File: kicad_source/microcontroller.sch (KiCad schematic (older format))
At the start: 47 parts, among them CN1 Micro_SDCard, CN2 CONN_02X05, CN5 CONN_01X04, CN6 CONN_01X04, SW1 TAST_VER, SW2 TAST_VER, SW3 TAST_VER, SW4 TAST_VER, U1 W25Q80D, U2 ATECC608A, U3 FE310-G002, U8 BMA400, Y1 16MHz

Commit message: changed JTAG connector
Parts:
- CN2: footprint pin_headers:Pin_Header_Straight_2x05_Pitch1.27mm -> CON_samtec:FSH-105-04-L-DH-SL
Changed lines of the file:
@@
 F 0 "CN2" H 5600 6015 50  0000 C CNN
 F 1 "CONN_02X05" H 5600 5924 50  0000 C CNN
-F 2 "pin_headers:Pin_Header_Straight_2x05_Pitch1.27mm" H 5600 5600 50  0001 C CNN
+F 2 "CON_samtec:FSH-105-04-L-DH-SL" H 5600 5600 50  0001 C CNN
 F 3 "" H 5600 4400 50  0000 C CNN
 	1    5600 5600

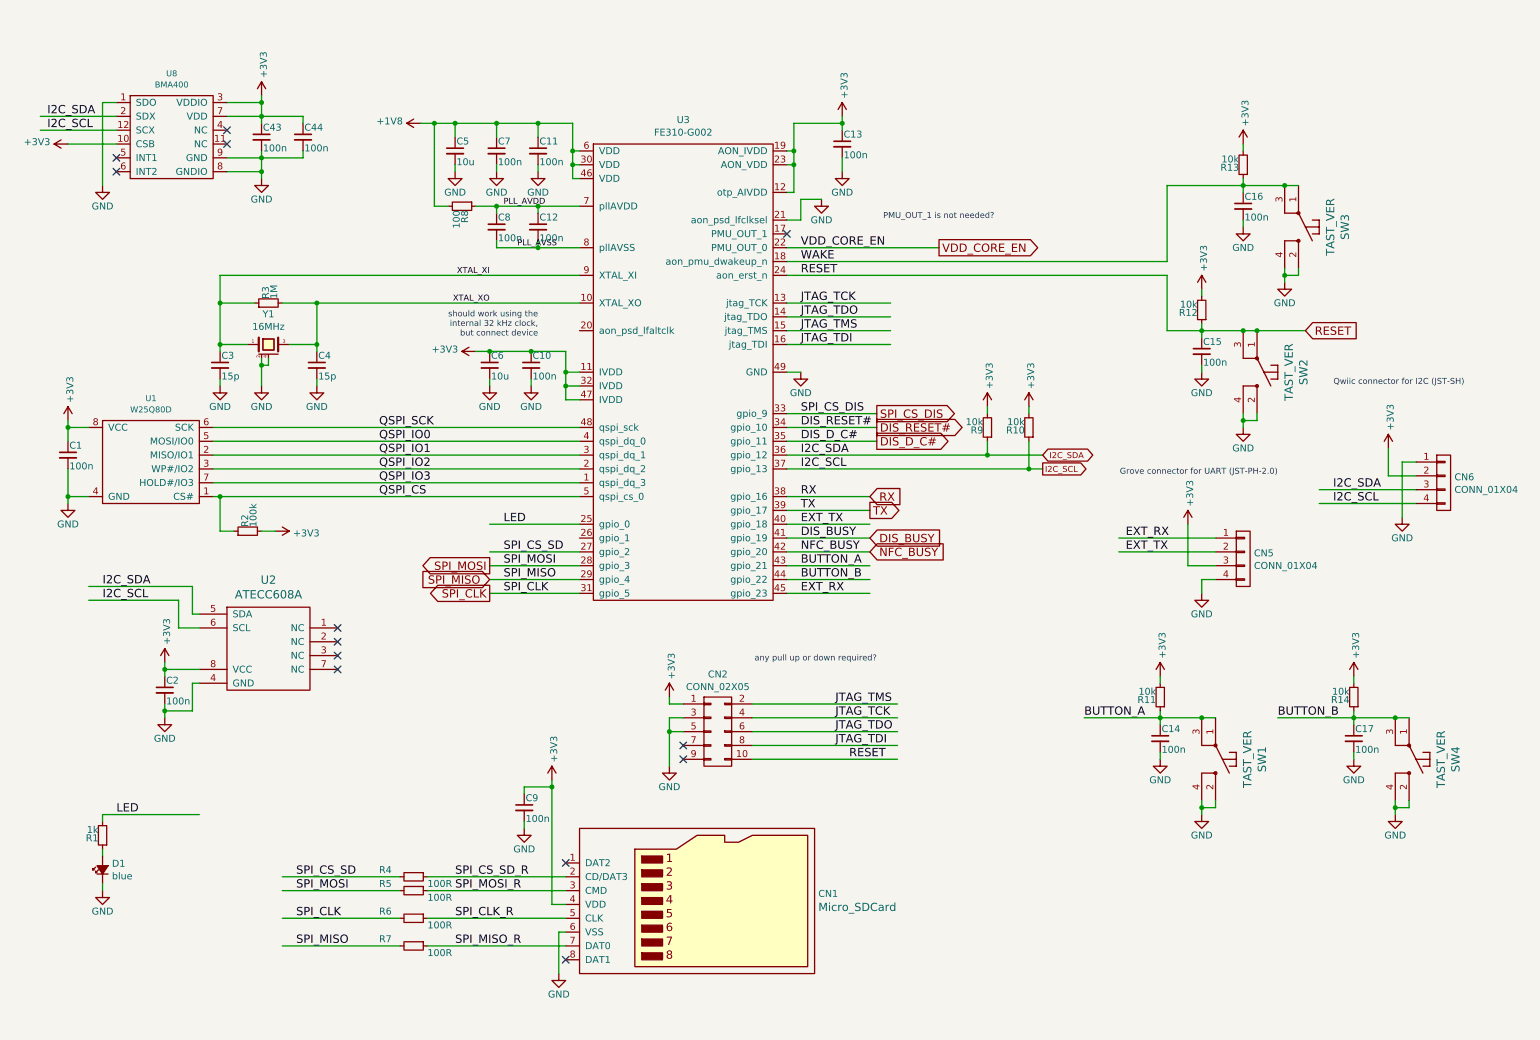
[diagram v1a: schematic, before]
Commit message: used small side switch for reset, added expansion connector,changed mounting holes
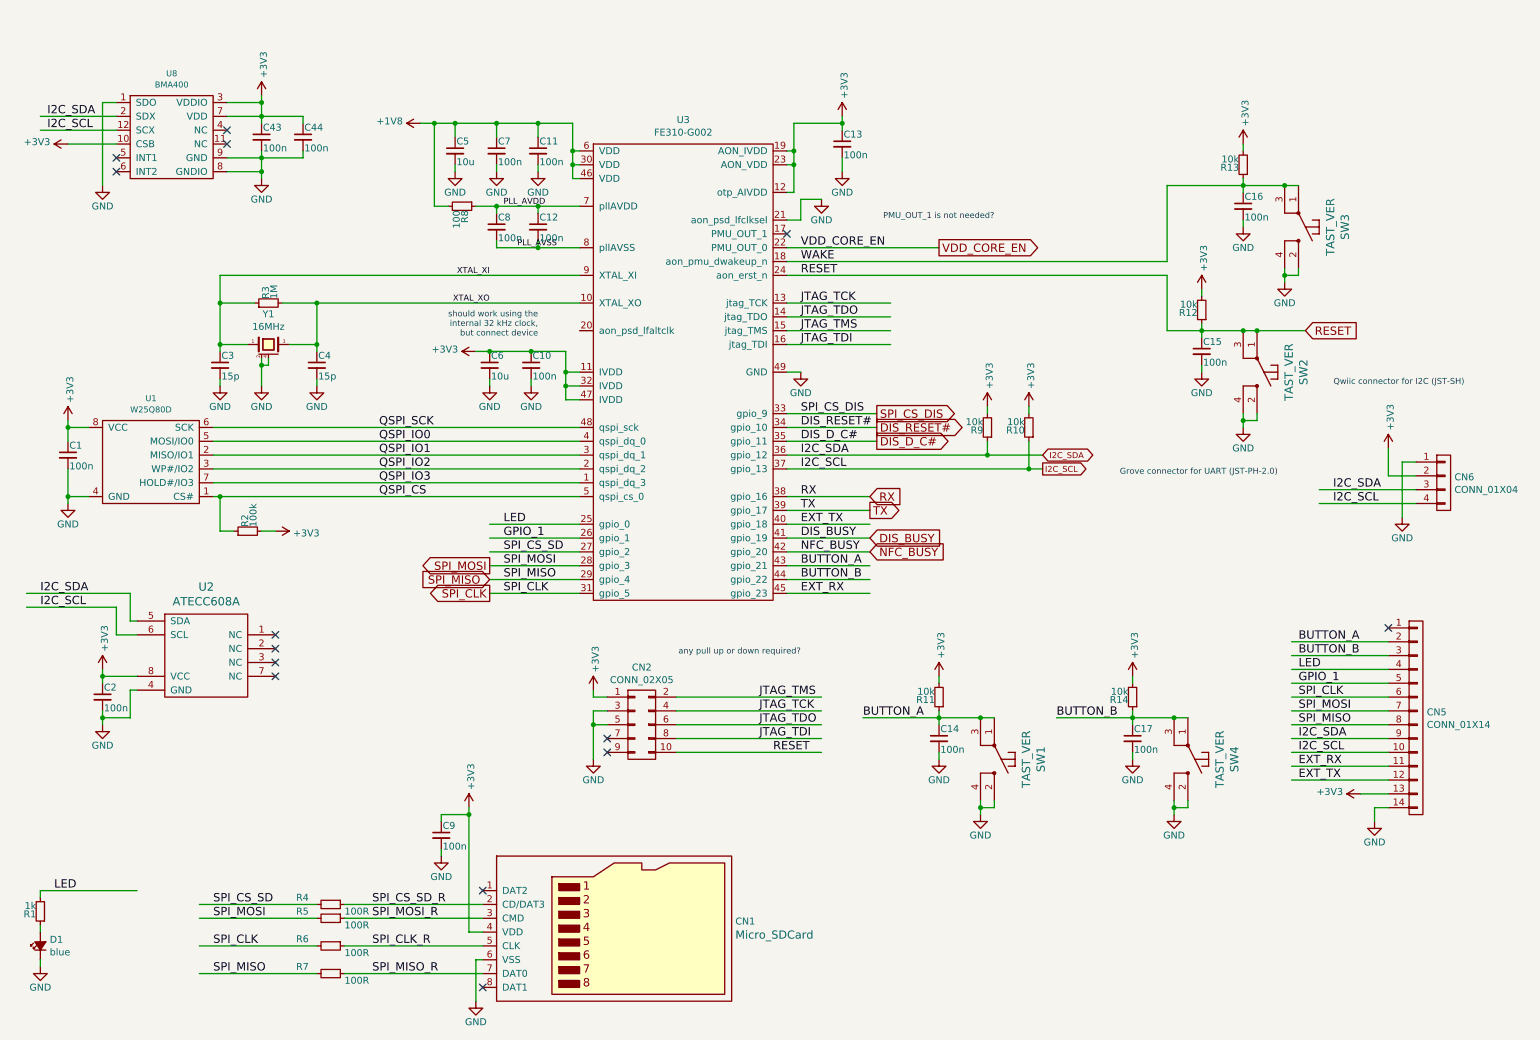
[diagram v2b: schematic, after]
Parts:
- removed CN5: CONN_01X04, connectors_JST_PH:Connectors_JST_S4B-PH-SM4-TB, symbol mechanical-connectors:CONN_01X04
- added CN5: CONN_01X14, CON_samtec:SIB-114-02-F-S_MATING, symbol mechanical-connectors:CONN_01X14
- SW2: footprint mechanical-switches:WE_430182050816 -> mechanical-switches:WE_434351045816
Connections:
- net labels added: GPIO_1
- wire segments 240 -> 249
- no-connect marks 13 -> 14
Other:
- moved on the sheet: C14, C17, C2, C9, CN1, CN2, D1, R1, R11, R14, R4, R5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

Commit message: changed to smaller crystal footprint
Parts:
- Y1: footprint crystals:Crystal_SMD_0603_4Pads -> crystals:Crystal_SMD_3.2x2.5mm_4Pad
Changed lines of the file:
@@
 F 0 "Y1" H 2350 3020 50  0000 C CNN
 F 1 "16MHz" H 2350 2929 50  0000 C CNN
-F 2 "crystals:Crystal_SMD_0603_4Pads" H 2350 2600 50  0001 C CNN
+F 2 "crystals:Crystal_SMD_3.2x2.5mm_4Pad" H 2350 2600 50  0001 C CNN
 F 3 "" H 2350 2800 50  0000 C CNN
 	1    2350 2800

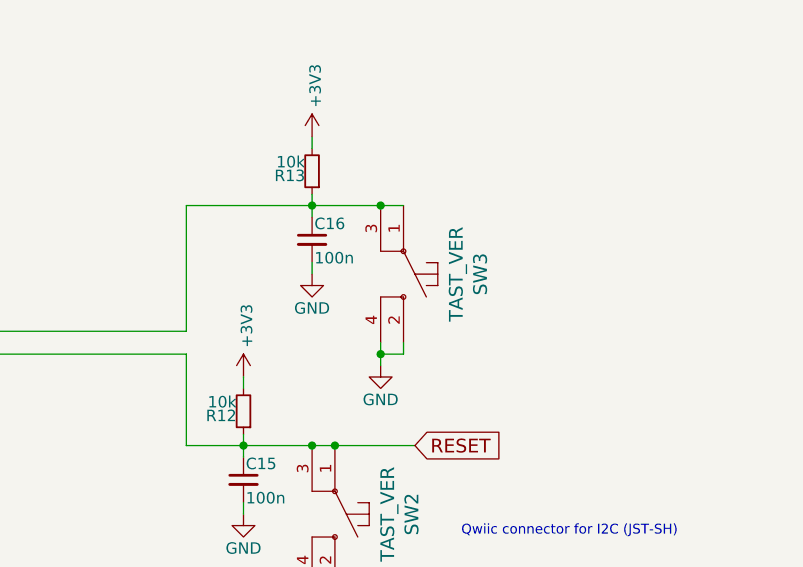
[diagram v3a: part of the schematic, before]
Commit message: changed wake button to smaller type, moved button A to left side, made some layout
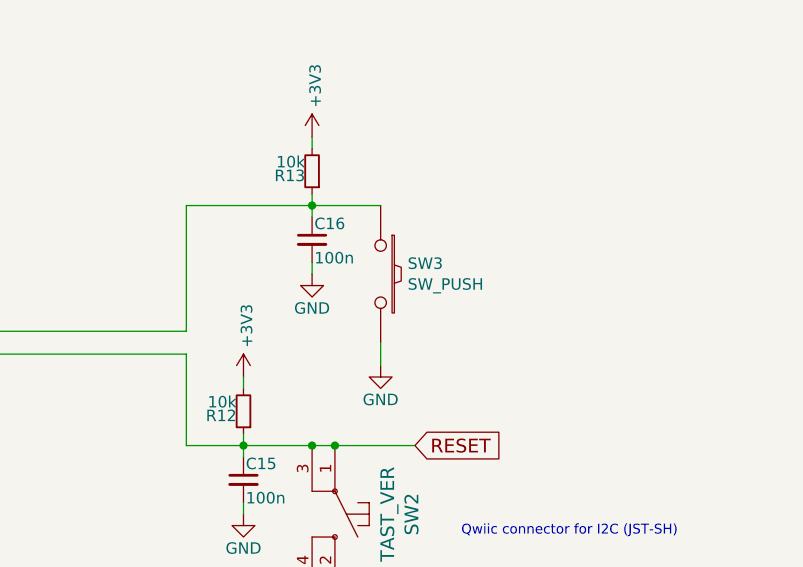
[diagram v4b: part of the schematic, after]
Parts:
- removed SW3: TAST_VER, mechanical-switches:WE_430182050816, symbol mechanical-switches:TAST_VER
- added SW3: SW_PUSH, mechanical-switches:smd_push, symbol devices:SW_PUSH
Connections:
- wire segments 249 -> 245
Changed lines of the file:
@@
 Wire Wire Line
 	9400 1900 9400 1950
-$Comp
-L mechanical-switches:TAST_VER SW3
-U 1 1 5EBE4535
-P 9800 1950
-F 0 "SW3" H 9800 2287 60  0000 C CNN
-F 1 "TAST_VER" H 9800 2181 60  0000 C CNN
-F 2 "mechanical-switches:WE_430182050816" H 10650 2000 60  0001 C CNN
-F 3 "" H 10650 2000 60  0000 C CNN
-	1    9800 1950
-	0    1    1    0
-$EndComp
 Wire Wire Line
 	9400 1600 9400 1650
@@
 Wire Wire Line
 	9400 1650 9400 1700
-Wire Wire Line
-	9700 1650 9400 1650
-Wire Wire Line
-	9800 1650 9700 1650
-Connection ~ 9700 1650
-Wire Wire Line
-	9700 2250 9700 2300
-Wire Wire Line
-	9700 2300 9800 2300
-Wire Wire Line
-	9800 2300 9800 2250
-Connection ~ 9700 2300
-Wire Wire Line
-	9700 2300 9700 2350
 $Comp
 L power-supply:GND #PWR033
@@
 BUTTON_A
 NoConn ~ 10450 4850
+Wire Wire Line
+	9400 1650 9700 1650
+$Comp
+L devices:SW_PUSH SW3
+U 1 1 5EE13CDC
+P 9700 1950
+F 0 "SW3" V 9654 2068 50  0000 L CNN
+F 1 "SW_PUSH" V 9745 2068 50  0000 L CNN
+F 2 "mechanical-switches:smd_push" V 9791 2068 50  0001 L CNN
+F 3 "" H 9700 1950 50  0000 C CNN
+	1    9700 1950
+	0    1    1    0
+$EndComp
+Wire Wire Line
+	9700 2250 9700 2350
 $EndSCHEMATC
